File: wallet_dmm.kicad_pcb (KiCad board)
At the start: 2 copper layers, 86 x 53 mm, 26 parts, among them J1 Conn_01x04, J2 Conn_01x02, Q1 T2N7002BK_LM, Q2 T2N7002BK_LM, SW1 RESET_BUTTON, SW2 BUTTON0, SW3 BUTTON1, SW4 BUTTON2, U1 STM32L051K8Tx, U2 TLC555xD, U3 MCP9700-E/TO

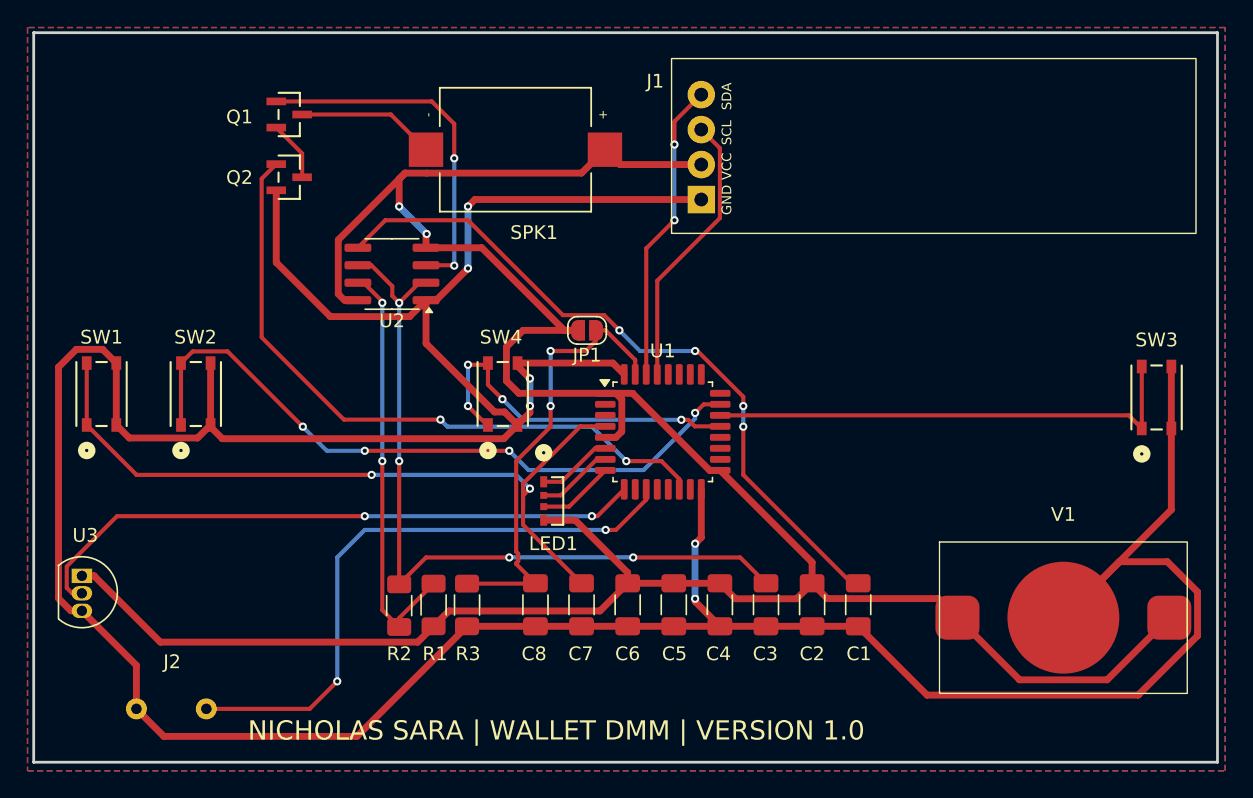
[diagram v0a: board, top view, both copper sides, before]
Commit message: Changed vias to 0.7 hole diameter and 0.9 diameter.
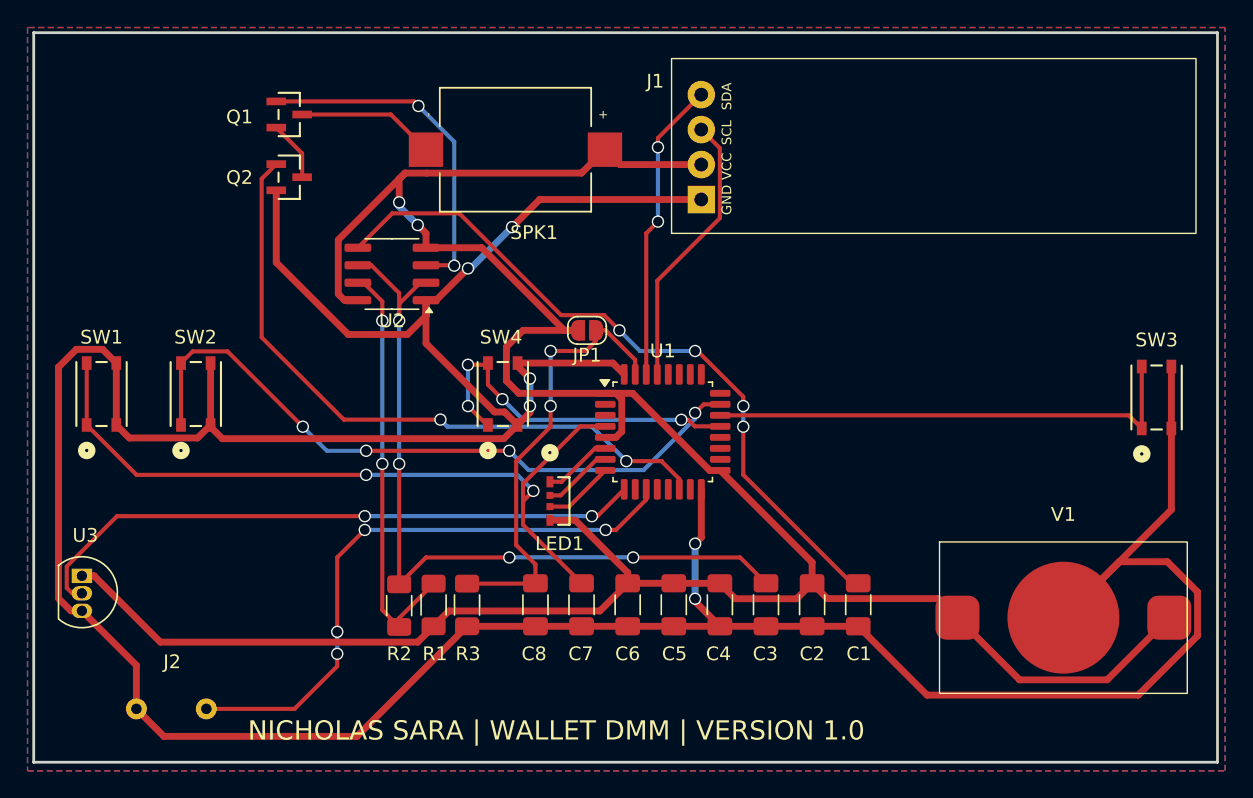
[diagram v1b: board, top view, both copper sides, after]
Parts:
- moved LED1 0.45 mm to (108.6, 62.9)
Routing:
- net Net-(U2-THR): track 55.8 -> 57.0 mm
- net GND: track 275.1 -> 274.2 mm
- net OSC_OUT: track 26.0 -> 25.2 mm
- net ADC: track 44.3 -> 43.6 mm, vias 2 -> 4
